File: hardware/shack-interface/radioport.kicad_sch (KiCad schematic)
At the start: 57 parts, among them U201 74LVC1G08, U202 74LVC1G08, U203 TLP4176G, U204 TLP176AM, U205 PC817X

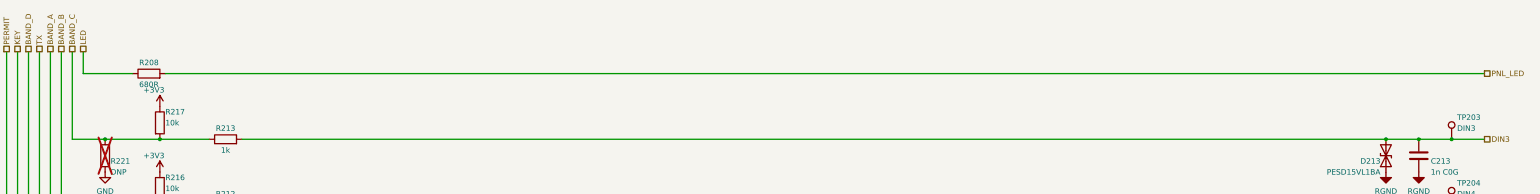
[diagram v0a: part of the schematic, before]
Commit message: Shack interface: end plates, schematic and PCB update; design log
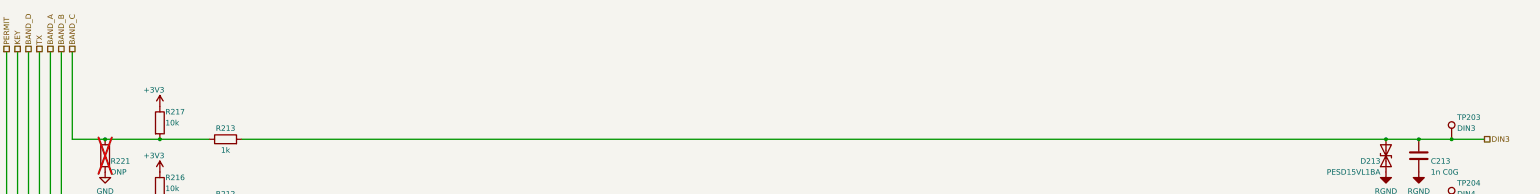
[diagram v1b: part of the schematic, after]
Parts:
- removed R208: 680R, Resistor_SMD:R_0603_1608Metric_Pad0.98x0.95mm_HandSolder, symbol Device:R
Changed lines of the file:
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@@
-	(symbol
-		(lib_id "Device:R")
-		(at 58.42 33.02 90)
-		(unit 1)
-		(body_style 1)
-		(exclude_from_sim no)
-		(in_bom yes)
-		(on_board yes)
-		(in_pos_files yes)
-		(dnp no)
-		(property "Reference" "R208"
-			(at 58.42 30.48 270)
-			(show_name no)
-			(do_not_autoplace no)
-			(effects
-				(font
-					(size 1.27 1.27)
-				)
-			)
-		)
-		(property "Value" "680R"
-			(at 58.42 35.56 270)
-			(show_name no)
-			(do_not_autoplace no)
-			(effects
-				(font
-					(size 1.27 1.27)
-				)
-			)
-		)
-		(property "Footprint" "Resistor_SMD:R_0603_1608Metric_Pad0.98x0.95mm_HandSolder"
-			(at 58.42 33.02 0)
-			(hide yes)
-			(show_name no)
-			(do_not_autoplace no)
-			(effects
-				(font
-					(size 1.27 1.27)
-				)
-				(justify left)
-			)
-		)
-		(property "Datasheet" ""
-			(at 58.42 33.02 0)
-			(hide yes)
-			(show_name no)
-			(do_not_autoplace no)
-			(effects
-				(font
-					(size 1.27 1.27)
-				)
-				(justify left)
-			)
-		)
-		(property "Description" "Panel LED about 2 mA"
-			(at 58.42 33.02 0)
-			(hide yes)
-			(show_name no)
-			(do_not_autoplace no)
-			(effects
-				(font
-					(size 1.27 1.27)
-				)
-				(justify left)
-			)
-		)
-		(pin "1"
-		)
-		(pin "2"
-		)
-		(instances
-			(project "shack-interface"
-				(path "/c90fc00c-0cb3-596c-9c35-501175caa333/ae66386f-fb37-57b6-95fd-c592663da00a"
-					(reference "R208")
-					(unit 1)
-				)
-				(path "/c90fc00c-0cb3-596c-9c35-501175caa333/ab2d0853-f823-5374-9e06-562bbb0786a4"
-					(reference "R308")
-					(unit 1)
-				)
-				(path "/c90fc00c-0cb3-596c-9c35-501175caa333/685ff83a-392d-50a5-9278-45d976e6a8d1"
-					(reference "R408")
-					(unit 1)
-				)
-			)
-		)
-	)
-	(hierarchical_label "LED"
-		(shape passive)
-		(at 43.18 27.94 90)
-		(effects
-			(font
-				(size 1.27 1.27)
-			)
-			(justify left)
-		)
-	)
-	(wire
-		(pts
-			(xy 43.18 27.94) (xy 43.18 33.02)
-		)
-		(stroke
-			(width 0)
-			(type default)
-		)
-	)
-	(wire
-		(pts
-			(xy 43.18 33.02) (xy 54.61 33.02)
-		)
-		(stroke
-			(width 0)
-			(type default)
-		)
-	)
-	(wire
-		(pts
-			(xy 62.23 33.02) (xy 368.3 33.02)
-		)
-		(stroke
-			(width 0)
-			(type default)
-		)
-	)
-	(hierarchical_label "PNL_LED"
-		(shape passive)
-		(at 368.3 33.02 0)
-		(effects
-			(font
-				(size 1.27 1.27)
-			)
-			(justify left)
-		)
-	)
 	(symbol
 		(lib_id "Device:R")
